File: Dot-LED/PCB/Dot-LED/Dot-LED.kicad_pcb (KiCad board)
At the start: 4 copper layers, 24.9 x 28 mm, 32 parts, among them CON1 SJ1-3523N, IC1 TPS631010YBGR, P1 USB_C_Plug, U1 ESP32-C3-MINI-1

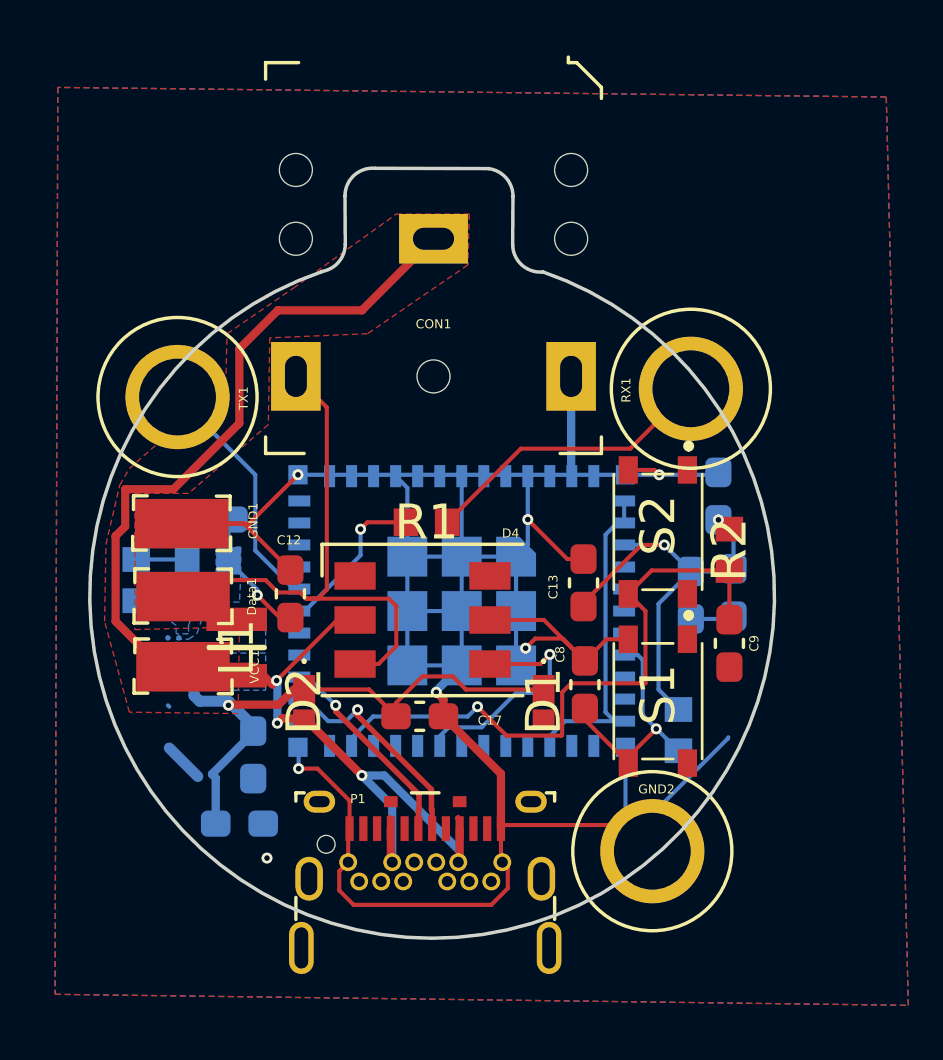
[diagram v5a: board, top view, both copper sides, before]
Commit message: finalize design based on in-stock parts
Gerber out 1.0
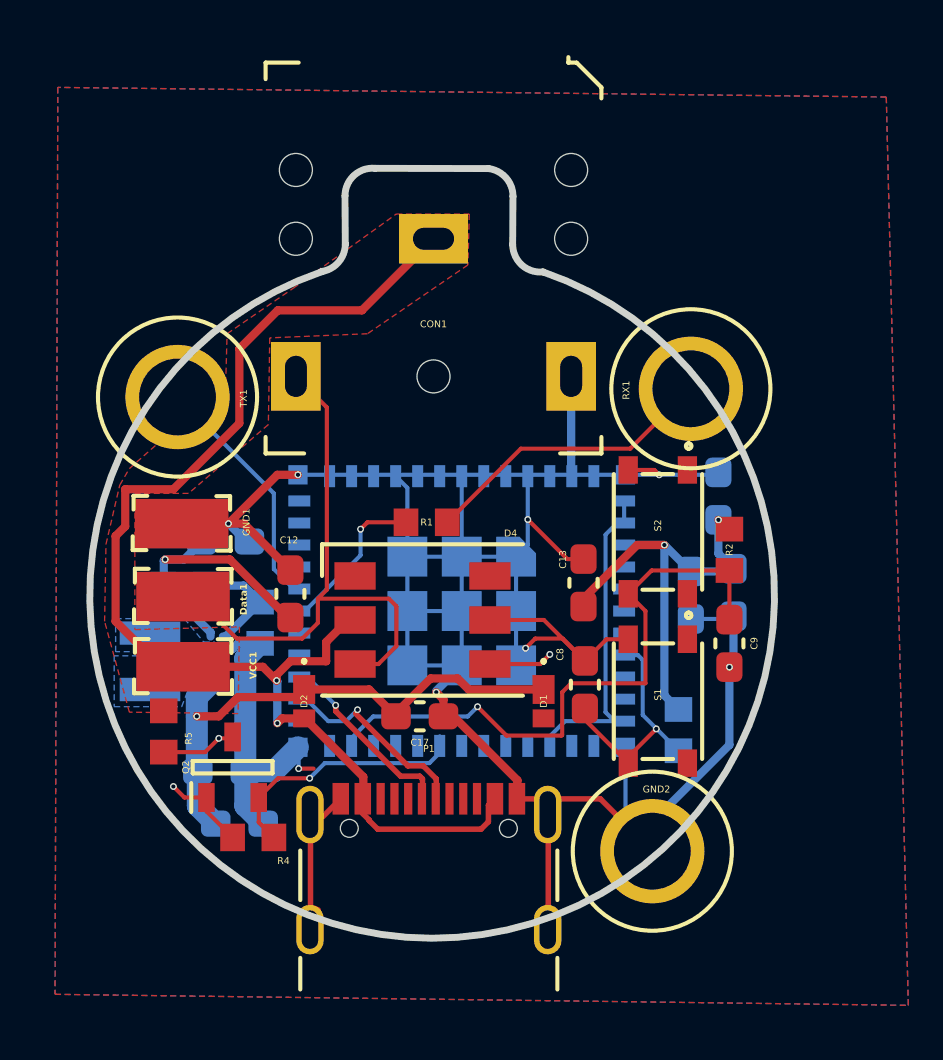
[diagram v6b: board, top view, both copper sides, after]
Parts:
- added Q2: BSS138P,215, SamacSys_Parts:SOT95P230X110-3N, F.Cu at (119.8, 62.0)
- added R4: 15k, SamacSys_Parts:RESC1608X55N, F.Cu at (120.5, 64.5)
- added R5: 15k, SamacSys_Parts:RESC1608X55N, F.Cu at (117.2, 60.7)
- L1: moved to B.Cu
- P1: footprint digikey-footprints:USB-C_Female_E8124-015-01 -> Connector_USB:USB_C_Receptacle_GCT_USB4105-xx-A_16P_TopMnt_Horizontal
- moved R7 4.76 mm to (120.8, 56.8)
- moved L1 3.19 mm to (116.8, 58.1), turned to 90 degrees
- moved P1 2.60 mm to (126.9, 66.8)
- moved IC1 1.55 mm to (119.2, 57.9)
- moved C18 1.30 mm to (119.3, 62.1), turned to 180 degrees
- moved R6 1.24 mm to (118.0, 55.4), turned to 0 degrees
- moved C14 1.00 mm to (119.5, 53.8), turned to 0 degrees
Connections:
- net SW renamed 3V3_VCC
- D4 pad 4: D5 -> /ESP32C3_MCU/5V_DIN
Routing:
- net 3V3_VCC: track 37.1 -> 60.2 mm, vias 3 -> 4
- net /ESP32C3_MCU/5V_DIN: track 0.00 -> 18.3 mm, vias 0 -> 2
- net GND: track 113.7 -> 124.1 mm, vias 7 -> 8
- net 5V: track 49.1 -> 46.1 mm, vias 3 -> 2
- net L1: track 0.00 -> 2.67 mm
- net Net-(IC1-LX2): track 0.00 -> 2.42 mm
- net Net-(IC1-FB): track 1.87 -> 4.12 mm
- net VIN: track 22.3 -> 20.6 mm
- net D5_out: track 20.7 -> 22.4 mm
- net D5: track 8.59 -> 9.53 mm
- net /ESP32C3_MCU/ESP_DN: track 7.95 -> 7.26 mm
- net /ESP32C3_MCU/ESP_DP: track 7.49 -> 6.86 mm
- added copper zone on B.Cu, net L1
- added copper zone on B.Cu, net Net-(IC1-LX2)
- removed copper zone on B.Cu, net (none)
- removed copper zone on B.Cu, net 3V3_VCC
- removed copper zone on B.Cu, net VIN

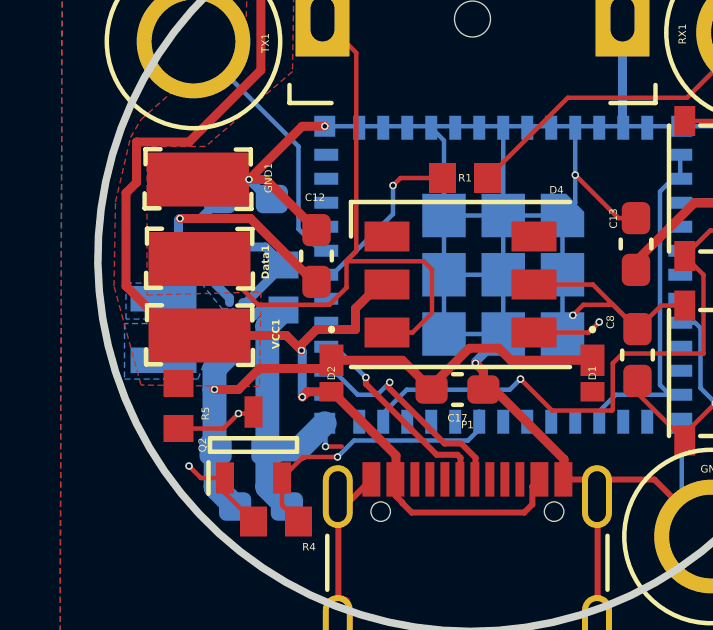
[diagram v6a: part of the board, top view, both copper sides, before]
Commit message: complete 0v1 layout aquarium
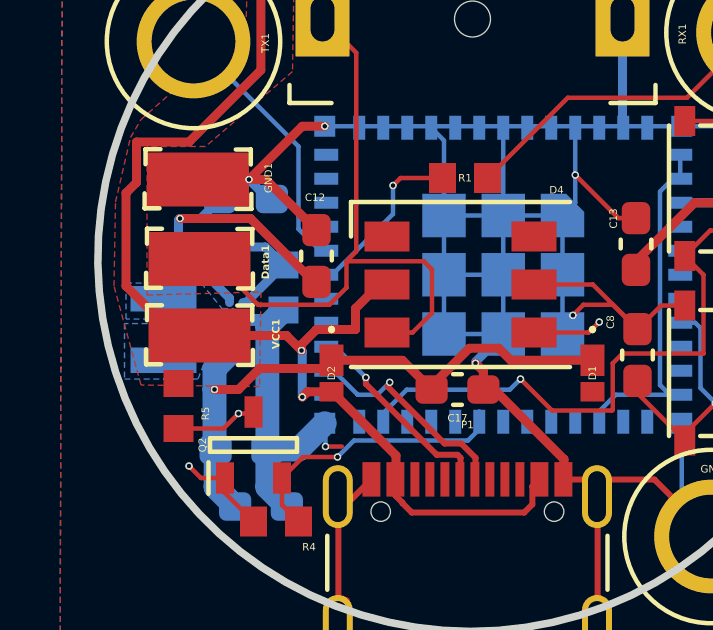
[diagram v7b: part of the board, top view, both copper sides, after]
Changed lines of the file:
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@@
     (pad_to_mask_clearance 0.05)
     (pcbplotparams
-      (layerselection 0x00010fc_fffffff9)
+      (layerselection 0x00010fc_ffffffff)
       (plot_on_all_layers_selection 0x0000000_00000000)
       (disableapertmacros false)
@@
   (segment (start 134.025 64.030047) (end 134.800649 64.805696) (width 0.15) (layer "B.Cu") (net 1))
   (segment (start 126.1 54.35) (end 126.1 51.85) (width 0.15) (layer "B.Cu") (net 1))
+  (segment (start 120.418199 57.831801) (end 119.368198 57.831801) (width 0.4) (layer "B.Cu") (net 1))
   (segment (start 126.1 51.85) (end 125.675 51.425) (width 0.15) (layer "B.Cu") (net 1))
+  (segment (start 120.75 57.5) (end 120.418199 57.831801) (width 0.4) (layer "B.Cu") (net 1))
   (segment (start 137.3125 51.375) (end 137.4 51.2875) (width 0.15) (layer "B.Cu") (net 1))
   (segment (start 120.3625 53.8) (end 120.25 53.8) (width 0.3) (layer "B.Cu") (net 1))
   (segment (start 127.15 59.225) (end 128.075 58.3) (width 0.3) (layer "B.Cu") (net 1))
   (segment (start 126.1 58.3) (end 130.05 58.3) (width 0.15) (layer "B.Cu") (net 1))
-  (segment (start 119.75 57.7) (end 119.35 57.7) (width 0.3) (layer "B.Cu") (net 1))
   (segment (start 135.25 51.375) (end 137.3125 51.375) (width 0.15) (layer "B.Cu") (net 1))
   (segment (start 120.2125 62.15) (end 121.25 62.15) (width 0.8) (layer "B.Cu") (net 1))
@@
   (segment (start 120.2125 63.4) (end 120.8625 64.05) (width 0.8) (layer "B.Cu") (net 1))
   (segment (start 130.475 53) (end 130.475 51.425) (width 0.15) (layer "B.Cu") (net 1))
-  (segment (start 120.75 57.5) (end 119.95 57.5) (width 0.3) (layer "B.Cu") (net 1))
   (segment (start 134.025 61.275) (end 134.025 64.030047) (width 0.15) (layer "B.Cu") (net 1))
-  (segment (start 119.95 57.5) (end 119.75 57.7) (width 0.3) (layer "B.Cu") (net 1))
   (segment (start 121.25 62.15) (end 122.125 61.275) (width 0.8) (layer "B.Cu") (net 1))
   (segment (start 130.05 56.325) (end 130.05 54.35) (width 0.15) (layer "B.Cu") (net 1))
